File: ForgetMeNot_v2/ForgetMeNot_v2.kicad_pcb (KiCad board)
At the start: 4 copper layers, 22.3 x 32.6 mm, 44 parts, among them J1 Conn_01x04, SW1 SW_Push, U1 RP2040, U2 W25Q128JVS, U3 NCP1117, U4 LIS2HH12, U5 MCP1640x-xMC, Y1 Crystal_ABM8

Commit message: finished layout & tracing
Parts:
- added C22: 100n, Capacitor_SMD:C_0402_1005Metric, F.Cu at (141.0, 95.5)
- C11, C12, R4: moved to B.Cu
- C21, R8: moved to F.Cu
- SW1: footprint Button_Switch_SMD:SW_Push_1TS009xxxx-xxxx-xxxx_6x6x5mm -> Button_Switch_SMD:SW_SPST_PTS647_Sx38
- TP1: footprint TestPoint:TestPoint_THTPad_1.5x1.5mm_Drill0.7mm -> TestPoint:TestPoint_THTPad_1.0x1.0mm_Drill0.5mm
- TP2: footprint TestPoint:TestPoint_THTPad_1.5x1.5mm_Drill0.7mm -> TestPoint:TestPoint_THTPad_D1.0mm_Drill0.5mm
- moved J1 14.3 mm to (136.4, 94.9), turned to 90 degrees
- moved C12 12.6 mm to (141.3, 80.0)
- moved U4 12.2 mm to (133.3, 95.4), turned to -90 degrees
- moved C18 11.7 mm to (132.5, 97.7), turned to 90 degrees
- moved BT1 11.4 mm to (137.0, 106.0), turned to 0 degrees
- moved C19 11.0 mm to (133.5, 97.7), turned to 90 degrees
- moved C17 9.47 mm to (134.5, 97.7), turned to 90 degrees
- moved R9 9.07 mm to (142.4, 97.3), turned to 90 degrees
- moved R4 9.03 mm to (142.3, 80.8), turned to -90 degrees
- moved U2 7.83 mm to (140.3, 81.7), turned to 0 degrees
- moved TP1 7.74 mm to (145.6, 85.4)
- moved TP2 6.64 mm to (144.8, 96.6)
- moved C20 6.63 mm to (144.1, 100.7), turned to 0 degrees
- moved SW1 6.58 mm to (143.3, 101.4), turned to 90 degrees
- moved Y1 5.79 mm to (134.0, 83.0)
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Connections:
- U1 pad 14: /LED -> unconnected-(U1-GPIO11-Pad14)
- U1 pad 2: unconnected-(U1-GPIO0-Pad2) -> /LED
- U1 pad 27: unconnected-(U1-GPIO16-Pad27) -> /ACC_SDA
- U1 pad 28: unconnected-(U1-GPIO17-Pad28) -> /ACC_SDO
- U1 pad 29: /BUZZ -> /ACC_CS
- U1 pad 30: /ZERO -> /ACC_SCL
- U1 pad 31: /ACC_SDA -> /ACC_INT
- U1 pad 32: /ACC_SDO -> /BUZZ
- U1 pad 34: /ACC_CS -> /ZERO
- U1 pad 35: /ACC_SCL -> unconnected-(U1-GPIO23-Pad35)
- U1 pad 36: /ACC_INT -> unconnected-(U1-GPIO24-Pad36)
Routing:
- net +5V: track 29.6 -> 15.7 mm
- net +3.3V: track 137.8 -> 127.1 mm, vias 10 -> 13
- net Net-(BT1-+): track 38.9 -> 28.9 mm
- net GND: track 11.2 -> 21.0 mm, vias 83 -> 28
- net /ZERO: track 15.8 -> 8.63 mm
- net /ACC_SDA: track 10.2 -> 3.65 mm
- net /ACC_SDO: track 9.51 -> 2.98 mm
- net /ACC_CS: track 8.64 -> 2.86 mm
- net Net-(R4-Pad1): track 11.6 -> 6.55 mm
- net /ACC_SCL: track 7.80 -> 2.84 mm
- net /QSPI_SS: track 19.5 -> 14.7 mm, vias 0 -> 1
- net /QSPI_SD1: track 16.5 -> 12.0 mm, vias 0 -> 2
- net /ACC_INT: track 7.91 -> 3.49 mm
- net /LED: track 12.5 -> 16.8 mm, vias 0 -> 2
- net /QSPI_SD3: track 7.15 -> 11.4 mm
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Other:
- board size 22.3 x 32.6 mm -> 16 x 33 mm

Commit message: added more ground vias
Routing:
- net GND: vias 28 -> 41
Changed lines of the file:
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@@
+	)
+	(via
+		(at 131.84 109.57)
+		(size 0.6)
+		(drill 0.3)
+		(layers "F.Cu" "B.Cu")
+		(free yes)
+		(net 2)
 	)
 	(via
@@
 	)
 	(via
+		(at 132.38 102.97)
+		(size 0.6)
+		(drill 0.3)
+		(layers "F.Cu" "B.Cu")
+		(free yes)
+		(net 2)
+	)
+	(via
 		(at 138.4 90.2375)
 		(size 0.6)
@@
 	)
 	(via
+		(at 140 102.97)
+		(size 0.6)
+		(drill 0.3)
+		(layers "F.Cu" "B.Cu")
+		(free yes)
+		(net 2)
+	)
+	(via
 		(at 139.09 85.45)
 		(size 0.6)
@@
 	)
 	(via
+		(at 133.84 103.57)
+		(size 0.6)
+		(drill 0.3)
+		(layers "F.Cu" "B.Cu")
+		(free yes)
+		(net 2)
+	)
+	(via
+		(at 139.84 109.57)
+		(size 0.6)
+		(drill 0.3)
+		(layers "F.Cu" "B.Cu")
+		(free yes)
+		(net 2)
+	)
+	(via
 		(at 141.16 81.63)
 		(size 0.6)
@@
 	)
 	(via
+		(at 143.84 97.57)
+		(size 0.6)
+		(drill 0.3)
+		(layers "F.Cu" "B.Cu")
+		(free yes)
+		(net 2)
+	)
+	(via
 		(at 140.59 88.1025)
 		(size 0.6)
@@
 	)
 	(via
+		(at 141.84 109.57)
+		(size 0.6)
+		(drill 0.3)
+		(layers "F.Cu" "B.Cu")
+		(free yes)
+		(net 2)
+	)
+	(via
+		(at 143.84 99.57)
+		(size 0.6)
+		(drill 0.3)
+		(layers "F.Cu" "B.Cu")
+		(free yes)
+		(net 2)
+	)
+	(via
+		(at 131.84 101.57)
+		(size 0.6)
+		(drill 0.3)
+		(layers "F.Cu" "B.Cu")
+		(free yes)
+		(net 2)
+	)
+	(via
 		(at 136.665 83.62)
 		(size 0.6)
@@
 	)
 	(via
+		(at 145.08 95.35)
+		(size 0.6)
+		(drill 0.3)
+		(layers "F.Cu" "B.Cu")
+		(free yes)
+		(net 2)
+	)
+	(via
 		(at 133.33 80.1)
 		(size 0.6)
@@
 	)
 	(via
+		(at 145.08 105.51)
+		(size 0.6)
+		(drill 0.3)
+		(layers "F.Cu" "B.Cu")
+		(free yes)
+		(net 2)
+	)
+	(via
 		(at 138.4 88.1025)
 		(size 0.6)
@@
 	)
 	(via
+		(at 131.84 99.57)
+		(size 0.6)
+		(drill 0.3)
+		(layers "F.Cu" "B.Cu")
+		(free yes)
+		(net 2)
+	)
+	(via
 		(at 141.207897 84.492103)
+		(size 0.6)
+		(drill 0.3)
+		(layers "F.Cu" "B.Cu")
+		(free yes)
+		(net 2)
+	)
+	(via
+		(at 133.84 105.57)
 		(size 0.6)
 		(drill 0.3)
@@
 		)
 	)
+	(group "ViaStitching GND"
+		(members "5cdd74ed-2311-4418-90b9-acc5baace0c7" "8be79405-bfa7-4c1f-96b1-a3b39196fe1b"
+			"92cf146b-4e46-457d-b4b0-dc56588c2da6" "9ca6e1f6-aaeb-4f2a-9150-d91ef81c62bb"
+			"b22172c4-83a9-4edc-b5c8-d43015d48994" "b4527aca-fb72-4f2d-b315-749c77f52d4c"
+			"cc61a422-6740-42d0-8ead-61773d5d0e7a" "ef71084d-369e-4b4a-aa2c-6b06b3362172"
+			"f78be405-d9aa-4bf3-aaed-68747654d684"
+		)
+	)

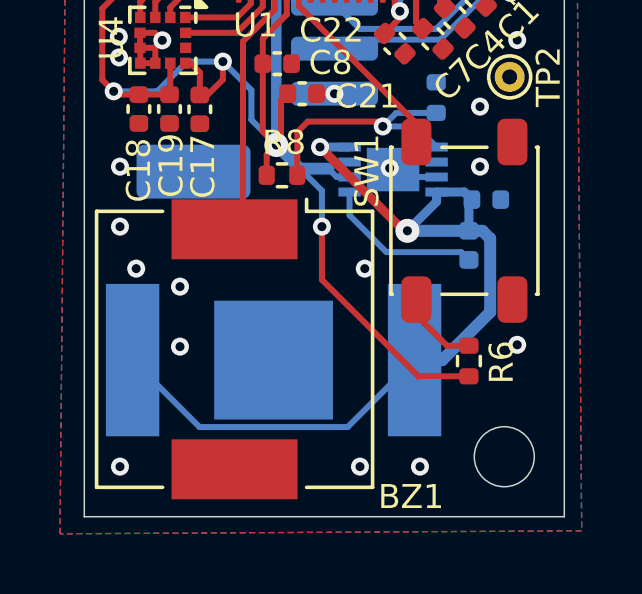
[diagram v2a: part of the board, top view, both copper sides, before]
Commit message: moved a resistor
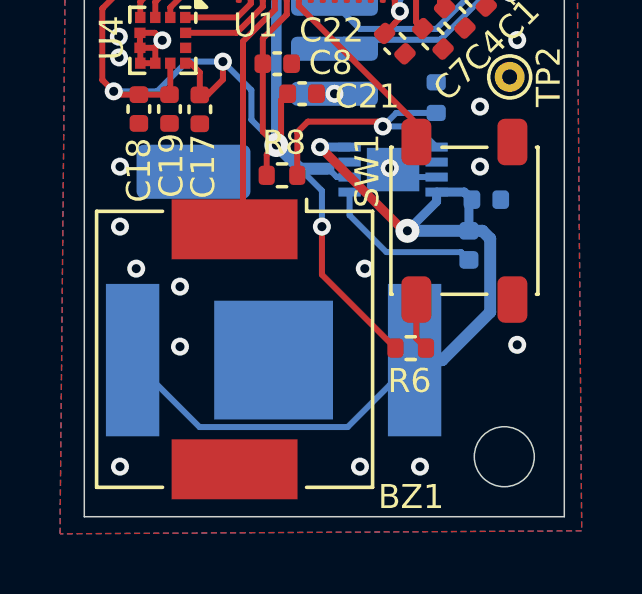
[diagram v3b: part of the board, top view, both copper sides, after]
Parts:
- moved R6 1.99 mm to (141.5, 105.6), turned to 0 degrees
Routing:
- net +3.3V: track 127.1 -> 124.1 mm
- net /ZERO: track 8.63 -> 7.69 mm
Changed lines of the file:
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@@
 	(footprint "Resistor_SMD:R_0402_1005Metric"
 		(layer "F.Cu")
-		(at 143.47 106.050001 90)
+		(at 141.530001 105.62)
 		(descr "Resistor SMD 0402 (1005 Metric), square (rectangular) end terminal, IPC-7351 nominal, (Body size source: IPC-SM-782 page 72, https://www.pcb-3d.com/wordpress/wp-content/uploads/ipc-sm-782a_amendment_1_and_2.pdf), generated with kicad-footprint-generator")
 		(tags "resistor")
 		(property "Reference" "R6"
-			(at -0.039999 1.09 90)
+			(at -0.039999 1.09 0)
 			(layer "F.SilkS")
 			(effects
@@
 		)
 		(property "Value" "10k"
-			(at -0.36 -1.25 90)
+			(at -0.36 -1.25 0)
 			(layer "F.Fab")
 			(effects
@@
 		)
 		(property "Datasheet" "~"
-			(at 0 0 90)
+			(at 0 0 0)
 			(layer "F.Fab")
 			(hide yes)
@@
 		)
 		(property "Description" "Resistor"
-			(at 0 0 90)
+			(at 0 0 0)
 			(layer "F.Fab")
 			(hide yes)
@@
 		)
 		(fp_line
-			(start 0.93 -0.47)
-			(end 0.93 0.47)
+			(start -0.93 -0.47)
+			(end 0.93 -0.47)
 			(stroke
 				(width 0.05)
@@
 		)
 		(fp_line
-			(start -0.93 -0.47)
-			(end 0.93 -0.47)
+			(start -0.93 0.47)
+			(end -0.93 -0.47)
 			(stroke
 				(width 0.05)
@@
 		)
 		(fp_line
-			(start 0.93 0.47)
-			(end -0.93 0.47)
+			(start 0.93 -0.47)
+			(end 0.93 0.47)
 			(stroke
 				(width 0.05)
@@
 		)
 		(fp_line
-			(start -0.93 0.47)
-			(end -0.93 -0.47)
+			(start 0.93 0.47)
+			(end -0.93 0.47)
 			(stroke
 				(width 0.05)
@@
 		)
 		(fp_line
-			(start 0.525 -0.27)
-			(end 0.525 0.27)
+			(start -0.525 -0.27)
+			(end 0.525 -0.27)
 			(stroke
 				(width 0.1)
@@
 		)
 		(fp_line
-			(start -0.525 -0.27)
-			(end 0.525 -0.27)
+			(start -0.525 0.27)
+			(end -0.525 -0.27)
 			(stroke
 				(width 0.1)
@@
 		)
 		(fp_line
-			(start 0.525 0.27)
-			(end -0.525 0.27)
+			(start 0.525 -0.27)
+			(end 0.525 0.27)
 			(stroke
 				(width 0.1)
@@
 		)
 		(fp_line
-			(start -0.525 0.27)
-			(end -0.525 -0.27)
+			(start 0.525 0.27)
+			(end -0.525 0.27)
 			(stroke
 				(width 0.1)
@@
 		)
 		(fp_text user "${REFERENCE}"
-			(at 0 0 90)
+			(at 0 0 0)
 			(layer "F.Fab")
 			(effects
@@
 		)
 		(pad "1" smd roundrect
-			(at -0.509999 0 90)
+			(at -0.509999 0)
 			(size 0.54 0.64)
 			(layers "F.Cu" "F.Mask" "F.Paste")
@@
 		)
 		(pad "2" smd roundrect
-			(at 0.509999 0 90)
+			(at 0.509999 0)
 			(size 0.54 0.64)
 			(layers "F.Cu" "F.Mask" "F.Paste")
@@
 	)
 	(segment
+		(start 138.57 103.169998)
+		(end 138.57 101.57)
+		(width 0.2)
+		(layer "F.Cu")
+		(net 1)
+	)
+	(segment
 		(start 133.49 97.17)
 		(end 132.47 97.17)
@@
 	)
 	(segment
-		(start 143.47 106.56)
-		(end 141.79 106.56)
-		(width 0.2)
-		(layer "F.Cu")
-		(net 1)
-	)
-	(segment
 		(start 136.6 98.4)
 		(end 137.05 98.85)
@@
 	)
 	(segment
-		(start 138.57 103.34)
-		(end 138.57 101.57)
-		(width 0.2)
-		(layer "F.Cu")
-		(net 1)
-	)
-	(segment
 		(start 137.64 84.73)
 		(end 137.46 84.73)
@@
 	)
 	(segment
-		(start 141.79 106.56)
-		(end 138.57 103.34)
-		(width 0.2)
-		(layer "F.Cu")
-		(net 1)
-	)
-	(segment
 		(start 131.251 96.681)
 		(end 131.251 94.299)
@@
 	)
 	(segment
+		(start 141.020002 105.62)
+		(end 138.57 103.169998)
+		(width 0.2)
+		(layer "F.Cu")
+		(net 1)
+	)
+	(segment
 		(start 143.3 79.81)
 		(end 143.84 79.81)
@@
 	)
 	(segment
-		(start 142.740001 105.540002)
-		(end 143.47 105.540002)
+		(start 141.72 105.3)
+		(end 142.04 105.62)
 		(width 0.2)
 		(layer "F.Cu")
@@
 	(segment
 		(start 141.72 104)
-		(end 141.72 104.520001)
+		(end 141.72 105.3)
 		(width 0.2)
 		(layer "F.Cu")
@@
 		(width 0.2)
 		(layer "F.Cu")
-		(net 17)
-	)
-	(segment
-		(start 141.72 104.520001)
-		(end 142.740001 105.540002)
-		(width 0.2)
-		(layer "F.Cu")

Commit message: Updated inductor
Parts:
- L1: footprint Inductor_SMD:L_0402_1005Metric -> Inductor_SMD:L_1008_2520Metric
- moved L1 1.48 mm to (144.4, 103.3)
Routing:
- net Net-(BT1-+): track 28.9 -> 33.4 mm
- net Net-(U5-SW): track 5.37 -> 6.85 mm
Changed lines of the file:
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@@
 		)
 	)
-	(footprint "Inductor_SMD:L_0402_1005Metric"
+	(footprint "Inductor_SMD:L_1008_2520Metric"
 		(layer "B.Cu")
-		(at 143.47 102.195 -90)
-		(descr "Inductor SMD 0402 (1005 Metric), square (rectangular) end terminal, IPC-7351 nominal, (Body size source: http://www.tortai-tech.com/upload/download/2011102023233369053.pdf), generated with kicad-footprint-generator")
+		(at 144.43 103.325 -90)
+		(descr "Inductor SMD 1008 (2520 Metric), square (rectangular) end terminal, IPC-7351 nominal, (Body size source: https://ecsxtal.com/store/pdf/ECS-MPI2520-SMD-POWER-INDUCTOR.pdf), generated with kicad-footprint-generator")
 		(tags "inductor")
 		(property "Reference" "L1"
-			(at 0.105 -1.12 90)
+			(at 2.885 0.6 90)
 			(layer "B.SilkS")
 			(effects
 				(font
-					(size 0.8 0.8)
-					(thickness 0.1)
+					(size 1 1)
+					(thickness 0.15)
 				)
 				(justify mirror)
@@
 		)
 		(property "Value" "4.7uH"
-			(at 0 -1.17 90)
+			(at 0 -2.05 90)
 			(layer "B.Fab")
 			(effects
@@
 		(attr smd)
 		(fp_line
-			(start -0.93 0.47)
-			(end 0.93 0.47)
+			(start -0.261253 1.11)
+			(end 0.261253 1.11)
+			(stroke
+				(width 0.12)
+				(type solid)
+			)
+			(layer "B.SilkS")
+		)
+		(fp_line
+			(start -0.261253 -1.11)
+			(end 0.261253 -1.11)
+			(stroke
+				(width 0.12)
+				(type solid)
+			)
+			(layer "B.SilkS")
+		)
+		(fp_line
+			(start -1.95 1.35)
+			(end 1.95 1.35)
 			(stroke
 				(width 0.05)
@@
 		)
 		(fp_line
-			(start 0.93 0.47)
-			(end 0.93 -0.47)
+			(start 1.95 1.35)
+			(end 1.95 -1.35)
 			(stroke
 				(width 0.05)
@@
 		)
 		(fp_line
-			(start -0.93 -0.47)
-			(end -0.93 0.47)
+			(start -1.95 -1.35)
+			(end -1.95 1.35)
 			(stroke
 				(width 0.05)
@@
 		)
 		(fp_line
-			(start 0.93 -0.47)
-			(end -0.93 -0.47)
+			(start 1.95 -1.35)
+			(end -1.95 -1.35)
 			(stroke
 				(width 0.05)
@@
 		)
 		(fp_line
-			(start -0.5 0.25)
-			(end 0.5 0.25)
+			(start -1.25 1)
+			(end 1.25 1)
 			(stroke
 				(width 0.1)
@@
 		)
 		(fp_line
-			(start 0.5 0.25)
-			(end 0.5 -0.25)
+			(start 1.25 1)
+			(end 1.25 -1)
 			(stroke
 				(width 0.1)
@@
 		)
 		(fp_line
-			(start -0.5 -0.25)
-			(end -0.5 0.25)
+			(start -1.25 -1)
+			(end -1.25 1)
 			(stroke
 				(width 0.1)
@@
 		)
 		(fp_line
-			(start 0.5 -0.25)
-			(end -0.5 -0.25)
+			(start 1.25 -1)
+			(end -1.25 -1)
 			(stroke
 				(width 0.1)
@@
 			(effects
 				(font
-					(size 0.25 0.25)
-					(thickness 0.04)
+					(size 0.62 0.62)
+					(thickness 0.09)
 				)
 				(justify mirror)
@@
 		)
 		(pad "1" smd roundrect
-			(at -0.485 0 270)
-			(size 0.59 0.64)
+			(at -1.075 0 270)
+			(size 1.25 2.2)
 			(layers "B.Cu" "B.Mask" "B.Paste")
-			(roundrect_rratio 0.25)
+			(roundrect_rratio 0.2)
 			(net 50 "Net-(BT1-+)")
 			(pinfunction "1")
@@
 		)
 		(pad "2" smd roundrect
-			(at 0.485 0 270)
-			(size 0.59 0.64)
+			(at 1.075 0 270)
+			(size 1.25 2.2)
 			(layers "B.Cu" "B.Mask" "B.Paste")
-			(roundrect_rratio 0.25)
+			(roundrect_rratio 0.2)
 			(net 51 "Net-(U5-SW)")
 			(pinfunction "2")
@@
 		)
 		(embedded_fonts no)
-		(model "${KICAD9_3DMODEL_DIR}/Inductor_SMD.3dshapes/L_0402_1005Metric.step"
+		(model "${KICAD9_3DMODEL_DIR}/Inductor_SMD.3dshapes/L_1008_2520Metric.step"
 			(offset
 				(xyz 0 0 0)
@@
 	)
 	(via
-		(at 145.08 105.51)
+		(at 145.54 106.97)
 		(size 0.6)
 		(drill 0.3)
@@
 	)
 	(segment
-		(start 142.58 106.02)
-		(end 141.66 106.02)
-		(width 0.4)
+		(start 146 105.36)
+		(end 145.77 105.59)
+		(width 0.3)
 		(layer "B.Cu")
 		(net 50)
@@
 	)
 	(segment
-		(start 143.47 101.71)
-		(end 143.92 101.71)
-		(width 0.4)
+		(start 142.3925 100.4175)
+		(end 143.3175 100.4175)
+		(width 0.3)
 		(layer "B.Cu")
 		(net 50)
 	)
 	(segment
-		(start 144.18 104.42)
-		(end 142.58 106.02)
+		(start 141.42 101.71)
+		(end 141.81 102.1)
 		(width 0.4)
 		(layer "B.Cu")
@@
 	)
 	(segment
-		(start 142.3925 100.4175)
-		(end 143.3175 100.4175)
-		(width 0.3)
-		(layer "B.Cu")
-		(net 50)
-	)
-	(segment
-		(start 143.47 101.71)
-		(end 143.47 100.77)
+		(start 144.01 102.25)
+		(end 144.43 102.25)
 		(width 0.3)
 		(layer "B.Cu")
@@
 	)
 	(segment
-		(start 144.18 101.97)
-		(end 144.18 104.42)
+		(start 144.28 102.1)
+		(end 144.43 102.25)
 		(width 0.4)
 		(layer "B.Cu")
@@
 	)
 	(segment
+		(start 143.57 101.39)
+		(end 144.43 102.25)
+		(width 0.3)
+		(layer "B.Cu")
+		(net 50)
+	)
+	(segment
+		(start 146 103.82)
+		(end 146 105.36)
+		(width 0.3)
+		(layer "B.Cu")
+		(net 50)
+	)
+	(segment
 		(start 132.26 106.02)
 		(end 134.491 108.251)
@@
 	)
 	(segment
-		(start 143.92 101.71)
-		(end 144.18 101.97)
-		(width 0.4)
+		(start 145.77 105.59)
+		(end 142.09 105.59)
+		(width 0.3)
 		(layer "B.Cu")
 		(net 50)
 	)
 	(segment
-		(start 141.42 101.71)
-		(end 143.47 101.71)
+		(start 144.43 102.25)
+		(end 146 103.82)
+		(width 0.3)
+		(layer "B.Cu")
+		(net 50)
+	)
+	(segment
+		(start 142.09 105.59)
+		(end 141.66 106.02)
+		(width 0.3)
+		(layer "B.Cu")
+		(net 50)
+	)
+	(segment
+		(start 141.81 102.1)
+		(end 144.28 102.1)
 		(width 0.4)
 		(layer "B.Cu")
@@
 	)
 	(segment
+		(start 143.57 100.67)
+		(end 143.57 101.39)
+		(width 0.3)
+		(layer "B.Cu")
+		(net 50)
+	)
+	(segment
 		(start 139.429 108.251)
 		(end 141.66 106.02)
@@
 	)
 	(segment
-		(start 143.21 102.42)
-		(end 140.72 102.42)
+		(start 144.43 104.4)
+		(end 142.71 102.68)
 		(width 0.2)
 		(layer "B.Cu")
@@
 	)
 	(segment
-		(start 143.47 102.68)
-		(end 143.21 102.42)
+		(start 139.4925 100.8625)
+		(end 139.4925 100.4175)
 		(width 0.2)
 		(layer "B.Cu")
@@
 	)
 	(segment
-		(start 139.4925 101.1925)
-		(end 139.4925 100.4175)
+		(start 142.71 102.68)
+		(end 141.31 102.68)
 		(width 0.2)
 		(layer "B.Cu")
@@
 	)
 	(segment
-		(start 140.72 102.42)
-		(end 139.4925 101.1925)
+		(start 141.31 102.68)
+		(end 139.4925 100.8625)
 		(width 0.2)
 		(layer "B.Cu")

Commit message: removed ncp1117 so that the board is always powered by the battery and not the case of sometimes powered by the usb. (reduces complexity)
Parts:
- removed the C11 at (144.7, 91.0)
- removed C15, C16: 10u, Capacitor_SMD:C_0402_1005Metric
- removed U3: NCP1117, Package_TO_SOT_SMD:SOT-223-3_TabPin2
- renumbered C22 to C11
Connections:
- J1 pad 4: +5V -> /VBUS
- U1 pad 48: +3.3V -> /VBUS
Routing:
- net +3.3V: track 124.1 -> 102.0 mm, vias 13 -> 12
- net +5V: track 15.7 -> 0.00 mm
- net /VBUS: track 0.00 -> 7.06 mm, vias 0 -> 1
- net +1V1: track 22.4 -> 23.8 mm
- net GND: vias 41 -> 42

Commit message: test points
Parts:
- added TP3: 3v3, TestPoint:TestPoint_THTPad_D1.0mm_Drill0.5mm, F.Cu at (143.4, 106.5)
- added TP4: SDA, TestPoint:TestPoint_Pad_D1.0mm, B.Cu at (132.1, 85.4)
- added TP5: SCL, TestPoint:TestPoint_Pad_D1.0mm, B.Cu at (134.8, 85.4)
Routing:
- net /ACC_SDA: track 3.65 -> 14.0 mm, vias 0 -> 1
- net /ACC_SCL: track 2.84 -> 12.9 mm, vias 0 -> 1
- net +3.3V: track 102.0 -> 105.0 mm
- net +1V1: track 23.8 -> 24.7 mm
